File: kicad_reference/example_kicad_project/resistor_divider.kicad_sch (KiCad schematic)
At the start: 2 parts

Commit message: script to find components and place them in skidl script somewhat working
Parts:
- R1, R2: footprint (none) -> Resistor_SMD:R_0603_1608Metric
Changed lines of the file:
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@@
+	(symbol
+		(lib_id "Device:R")
+		(at 121.92 77.47 0)
+		(unit 1)
+		(exclude_from_sim no)
+		(in_bom yes)
+		(on_board yes)
+		(dnp no)
+		(fields_autoplaced yes)
+		(property "Reference" "R2"
+			(at 124.46 76.1999 0)
+			(effects
+				(font
+					(size 1.27 1.27)
+				)
+				(justify left)
+			)
+		)
+		(property "Value" "R"
+			(at 124.46 78.7399 0)
+			(effects
+				(font
+					(size 1.27 1.27)
+				)
+				(justify left)
+			)
+		)
+		(property "Footprint" "Resistor_SMD:R_0603_1608Metric"
+			(at 120.142 77.47 90)
+			(effects
+				(font
+					(size 1.27 1.27)
+				)
+				(hide yes)
+			)
+		)
+		(property "Datasheet" "~"
+			(at 121.92 77.47 0)
+			(effects
+				(font
+					(size 1.27 1.27)
+				)
+				(hide yes)
+			)
+		)
+		(property "Description" "Resistor"
+			(at 121.92 77.47 0)
+			(effects
+				(font
+					(size 1.27 1.27)
+				)
+				(hide yes)
+			)
+		)
+		(pin "2"
+		)
+		(pin "1"
+		)
+		(instances
+			(project "example_kicad_project"
+				(path "/139408cf-b4ac-4ccf-8751-afbb6def1f13/7dcd522d-d03d-41f6-bad3-56f1f937b049"
+					(reference "R2")
+					(unit 1)
+				)
+			)
+		)
+	)
 	(symbol
 		(lib_id "Device:R")
@@
 			)
 		)
-		(property "Footprint" ""
+		(property "Footprint" "Resistor_SMD:R_0603_1608Metric"
 			(at 120.142 63.5 90)
 			(effects
@@
 					(unit 1)
 				)
-			)
-		)
-	)
-	(symbol
-		(lib_id "Device:R")
-		(at 121.92 77.47 0)
-		(unit 1)
-		(exclude_from_sim no)
-		(in_bom yes)
-		(on_board yes)
-		(dnp no)
-		(fields_autoplaced yes)
-		(property "Reference" "R2"
-			(at 124.46 76.1999 0)
-			(effects
-				(font
-					(size 1.27 1.27)
-				)
-				(justify left)
-			)
-		)
-		(property "Value" "R"
-			(at 124.46 78.7399 0)
-			(effects
-				(font
-					(size 1.27 1.27)
-				)
-				(justify left)
-			)
-		)
-		(property "Footprint" ""
-			(at 120.142 77.47 90)
-			(effects
-				(font
-					(size 1.27 1.27)
-				)
-				(hide yes)
-			)
-		)
-		(property "Datasheet" "~"
-			(at 121.92 77.47 0)
-			(effects
-				(font
-					(size 1.27 1.27)
-				)
-				(hide yes)
-			)
-		)
-		(property "Description" "Resistor"
-			(at 121.92 77.47 0)
-			(effects
-				(font
-					(size 1.27 1.27)
-				)
-				(hide yes)
-			)
-		)
-		(pin "2"
-		)
-		(pin "1"
-		)
-		(instances
-			(project "example_kicad_project"
-				(path "/139408cf-b4ac-4ccf-8751-afbb6def1f13/7dcd522d-d03d-41f6-bad3-56f1f937b049"
-					(reference "R2")
-					(unit 1)
-				)

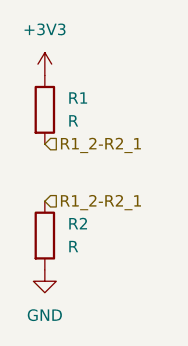
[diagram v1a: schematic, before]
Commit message: update resistor divider
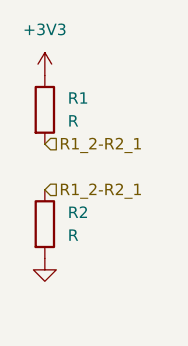
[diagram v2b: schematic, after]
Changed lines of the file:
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@@
 	(hierarchical_label "R1_2-R2_1"
 		(shape input)
-		(at 121.92 73.66 0)
+		(at 121.92 72.39 0)
 		(fields_autoplaced yes)
 		(effects
@@
 	(symbol
 		(lib_id "Device:R")
-		(at 121.92 77.47 0)
+		(at 121.92 63.5 0)
+		(unit 1)
+		(exclude_from_sim no)
+		(in_bom yes)
+		(on_board yes)
+		(dnp no)
+		(fields_autoplaced yes)
+		(property "Reference" "R1"
+			(at 124.46 62.2299 0)
+			(effects
+				(font
+					(size 1.27 1.27)
+				)
+				(justify left)
+			)
+		)
+		(property "Value" "R"
+			(at 124.46 64.7699 0)
+			(effects
+				(font
+					(size 1.27 1.27)
+				)
+				(justify left)
+			)
+		)
+		(property "Footprint" "Resistor_SMD:R_0603_1608Metric"
+			(at 120.142 63.5 90)
+			(effects
+				(font
+					(size 1.27 1.27)
+				)
+				(hide yes)
+			)
+		)
+		(property "Datasheet" "~"
+			(at 121.92 63.5 0)
+			(effects
+				(font
+					(size 1.27 1.27)
+				)
+				(hide yes)
+			)
+		)
+		(property "Description" "Resistor"
+			(at 121.92 63.5 0)
+			(effects
+				(font
+					(size 1.27 1.27)
+				)
+				(hide yes)
+			)
+		)
+		(pin "2"
+		)
+		(pin "1"
+		)
+		(instances
+			(project "example_kicad_project"
+				(path "/139408cf-b4ac-4ccf-8751-afbb6def1f13/7dcd522d-d03d-41f6-bad3-56f1f937b049"
+					(reference "R1")
+					(unit 1)
+				)
+			)
+		)
+	)
+	(symbol
+		(lib_id "power:+3V3")
+		(at 121.92 59.69 0)
+		(unit 1)
+		(exclude_from_sim no)
+		(in_bom yes)
+		(on_board yes)
+		(dnp no)
+		(fields_autoplaced yes)
+		(property "Reference" "#PWR04"
+			(at 121.92 63.5 0)
+			(effects
+				(font
+					(size 1.27 1.27)
+				)
+				(hide yes)
+			)
+		)
+		(property "Value" "+3V3"
+			(at 121.92 54.61 0)
+			(effects
+				(font
+					(size 1.27 1.27)
+				)
+			)
+		)
+		(property "Footprint" ""
+			(at 121.92 59.69 0)
+			(effects
+				(font
+					(size 1.27 1.27)
+				)
+				(hide yes)
+			)
+		)
+		(property "Datasheet" ""
+			(at 121.92 59.69 0)
+			(effects
+				(font
+					(size 1.27 1.27)
+				)
+				(hide yes)
+			)
+		)
+		(property "Description" "Power symbol creates a global label with name \"+3V3\""
+			(at 121.92 59.69 0)
+			(effects
+				(font
+					(size 1.27 1.27)
+				)
+				(hide yes)
+			)
+		)
+		(pin "1"
+		)
+		(instances
+			(project "example_kicad_project"
+				(path "/139408cf-b4ac-4ccf-8751-afbb6def1f13/7dcd522d-d03d-41f6-bad3-56f1f937b049"
+					(reference "#PWR04")
+					(unit 1)
+				)
+			)
+		)
+	)
+	(symbol
+		(lib_id "Device:R")
+		(at 121.92 76.2 0)
 		(unit 1)
 		(exclude_from_sim no)
@@
 		(fields_autoplaced yes)
 		(property "Reference" "R2"
-			(at 124.46 76.1999 0)
+			(at 124.46 74.9299 0)
 			(effects
 				(font
@@
 		)
 		(property "Value" "R"
-			(at 124.46 78.7399 0)
+			(at 124.46 77.4699 0)
 			(effects
 				(font
@@
 		)
 		(property "Footprint" "Resistor_SMD:R_0603_1608Metric"
-			(at 120.142 77.47 90)
+			(at 120.142 76.2 90)
 			(effects
 				(font
@@
 		)
 		(property "Datasheet" "~"
-			(at 121.92 77.47 0)
+			(at 121.92 76.2 0)
 			(effects
 				(font
@@
 		)
 		(property "Description" "Resistor"
-			(at 121.92 77.47 0)
+			(at 121.92 76.2 0)
 			(effects
 				(font
@@
 	)
 	(symbol
-		(lib_id "Device:R")
-		(at 121.92 63.5 0)
-		(unit 1)
-		(exclude_from_sim no)
-		(in_bom yes)
-		(on_board yes)
-		(dnp no)
-		(fields_autoplaced yes)
-		(property "Reference" "R1"
-			(at 124.46 62.2299 0)
-			(effects
-				(font
-					(size 1.27 1.27)
-				)
-				(justify left)
-			)
-		)
-		(property "Value" "R"
-			(at 124.46 64.7699 0)
-			(effects
-				(font
-					(size 1.27 1.27)
-				)
-				(justify left)
-			)
-		)
-		(property "Footprint" "Resistor_SMD:R_0603_1608Metric"
-			(at 120.142 63.5 90)
-			(effects
-				(font
-					(size 1.27 1.27)
-				)
-				(hide yes)
-			)
-		)
-		(property "Datasheet" "~"
-			(at 121.92 63.5 0)
-			(effects
-				(font
-					(size 1.27 1.27)
-				)
-				(hide yes)
-			)
-		)
-		(property "Description" "Resistor"
-			(at 121.92 63.5 0)
-			(effects
-				(font
-					(size 1.27 1.27)
-				)
-				(hide yes)
-			)
-		)
-		(pin "2"
-		)
-		(pin "1"
-		)
-		(instances
-			(project "example_kicad_project"
-				(path "/139408cf-b4ac-4ccf-8751-afbb6def1f13/7dcd522d-d03d-41f6-bad3-56f1f937b049"
-					(reference "R1")
-					(unit 1)
-				)
-			)
-		)
-	)
-	(symbol
-		(lib_id "power:+3V3")
-		(at 121.92 59.69 0)
-		(unit 1)
-		(exclude_from_sim no)
-		(in_bom yes)
-		(on_board yes)
-		(dnp no)
-		(fields_autoplaced yes)
-		(property "Reference" "#PWR04"
-			(at 121.92 63.5 0)
-			(effects
-				(font
-					(size 1.27 1.27)
-				)
-				(hide yes)
-			)
-		)
-		(property "Value" "+3V3"
-			(at 121.92 54.61 0)
-			(effects
-				(font
-					(size 1.27 1.27)
-				)
+		(lib_id "power:GND")
+		(at 121.92 80.01 0)
+		(unit 1)
+		(exclude_from_sim no)
+		(in_bom yes)
+		(on_board yes)
+		(dnp no)
+		(fields_autoplaced yes)
+		(property "Reference" "#PWR05"
+			(at 121.92 86.36 0)
+			(effects
+				(font
+					(size 1.27 1.27)
+				)
+				(hide yes)
+			)
+		)
+		(property "Value" "GND"
+			(at 121.92 85.09 0)
+			(effects
+				(font
+					(size 1.27 1.27)
+				)
+				(hide yes)
 			)
 		)
 		(property "Footprint" ""
-			(at 121.92 59.69 0)
+			(at 121.92 80.01 0)
 			(effects
 				(font
@@
 		)
 		(property "Datasheet" ""
-			(at 121.92 59.69 0)
-			(effects
-				(font
-					(size 1.27 1.27)
-				)
-				(hide yes)
-			)
-		)
-		(property "Description" "Power symbol creates a global label with name \"+3V3\""
-			(at 121.92 59.69 0)
-			(effects
-				(font
-					(size 1.27 1.27)
-				)
-				(hide yes)
-			)
-		)
-		(pin "1"
-		)
-		(instances
-			(project "example_kicad_project"
-				(path "/139408cf-b4ac-4ccf-8751-afbb6def1f13/7dcd522d-d03d-41f6-bad3-56f1f937b049"
-					(reference "#PWR04")
-					(unit 1)
-				)
-			)
-		)
-	)
-	(symbol
-		(lib_id "power:GND")
-		(at 121.92 81.28 0)
-		(unit 1)
-		(exclude_from_sim no)
-		(in_bom yes)
-		(on_board yes)
-		(dnp no)
-		(fields_autoplaced yes)
-		(property "Reference" "#PWR05"
-			(at 121.92 87.63 0)
-			(effects
-				(font
-					(size 1.27 1.27)
-				)
-				(hide yes)
-			)
-		)
-		(property "Value" "GND"
-			(at 121.92 86.36 0)
-			(effects
-				(font
-					(size 1.27 1.27)
-				)
-			)
-		)
-		(property "Footprint" ""
-			(at 121.92 81.28 0)
-			(effects
-				(font
-					(size 1.27 1.27)
-				)
-				(hide yes)
-			)
-		)
-		(property "Datasheet" ""
-			(at 121.92 81.28 0)
+			(at 121.92 80.01 0)
 			(effects
 				(font
@@
 		)
 		(property "Description" "Power symbol creates a global label with name \"GND\" , ground"
-			(at 121.92 81.28 0)
-			(effects
-				(font
-					(size 1.27 1.27)
-				)
-				(hide yes)
-			)
-		)
-		(pin "1"
-		)
-		(instances
-			(project "example_kicad_project"
+			(at 121.92 80.01 0)
+			(effects
+				(font
+					(size 1.27 1.27)
+				)
+				(hide yes)
+			)
+		)
+		(pin "1"
+		)
+		(instances
+			(project ""
 				(path "/139408cf-b4ac-4ccf-8751-afbb6def1f13/7dcd522d-d03d-41f6-bad3-56f1f937b049"
 					(reference "#PWR05")
